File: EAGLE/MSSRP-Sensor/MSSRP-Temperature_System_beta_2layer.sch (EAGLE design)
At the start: 175 parts, among them J1 POWER_JACKPTH, J10 BNCPTH, J11 BNCPTH, J2 USBSMD, J4 TE-2-TERMBLOCK, J5 TE-2-TERMBLOCK, J6 TE-2-TERMBLOCK, J7 TE-2-TERMBLOCK, J8 BNCPTH, J9 BNCPTH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

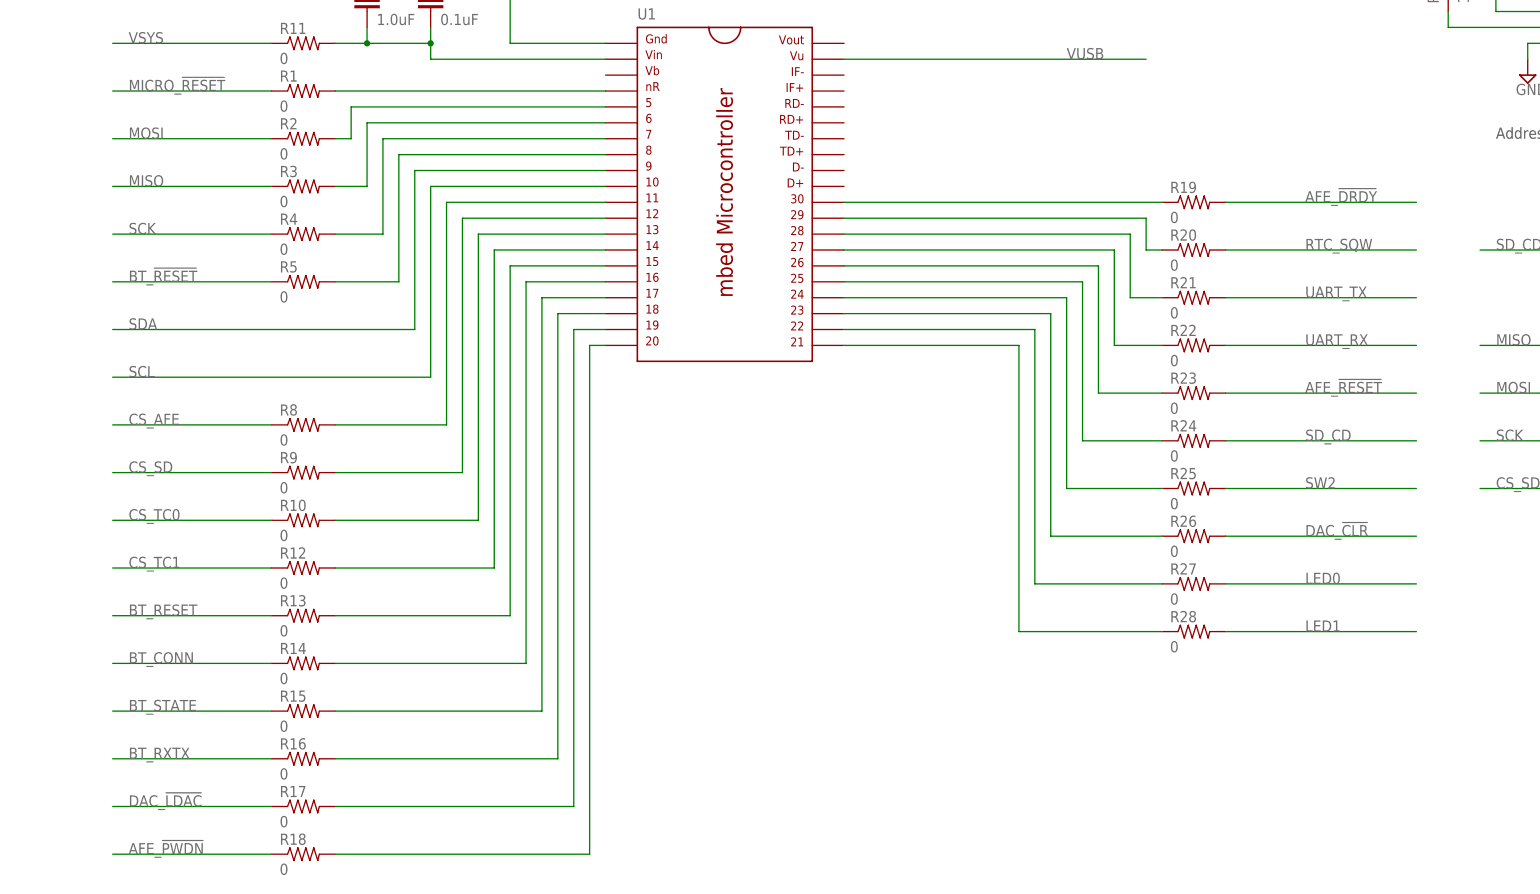
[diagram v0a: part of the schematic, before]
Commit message: 2-layer routing
Finished 2-layer routing tasks
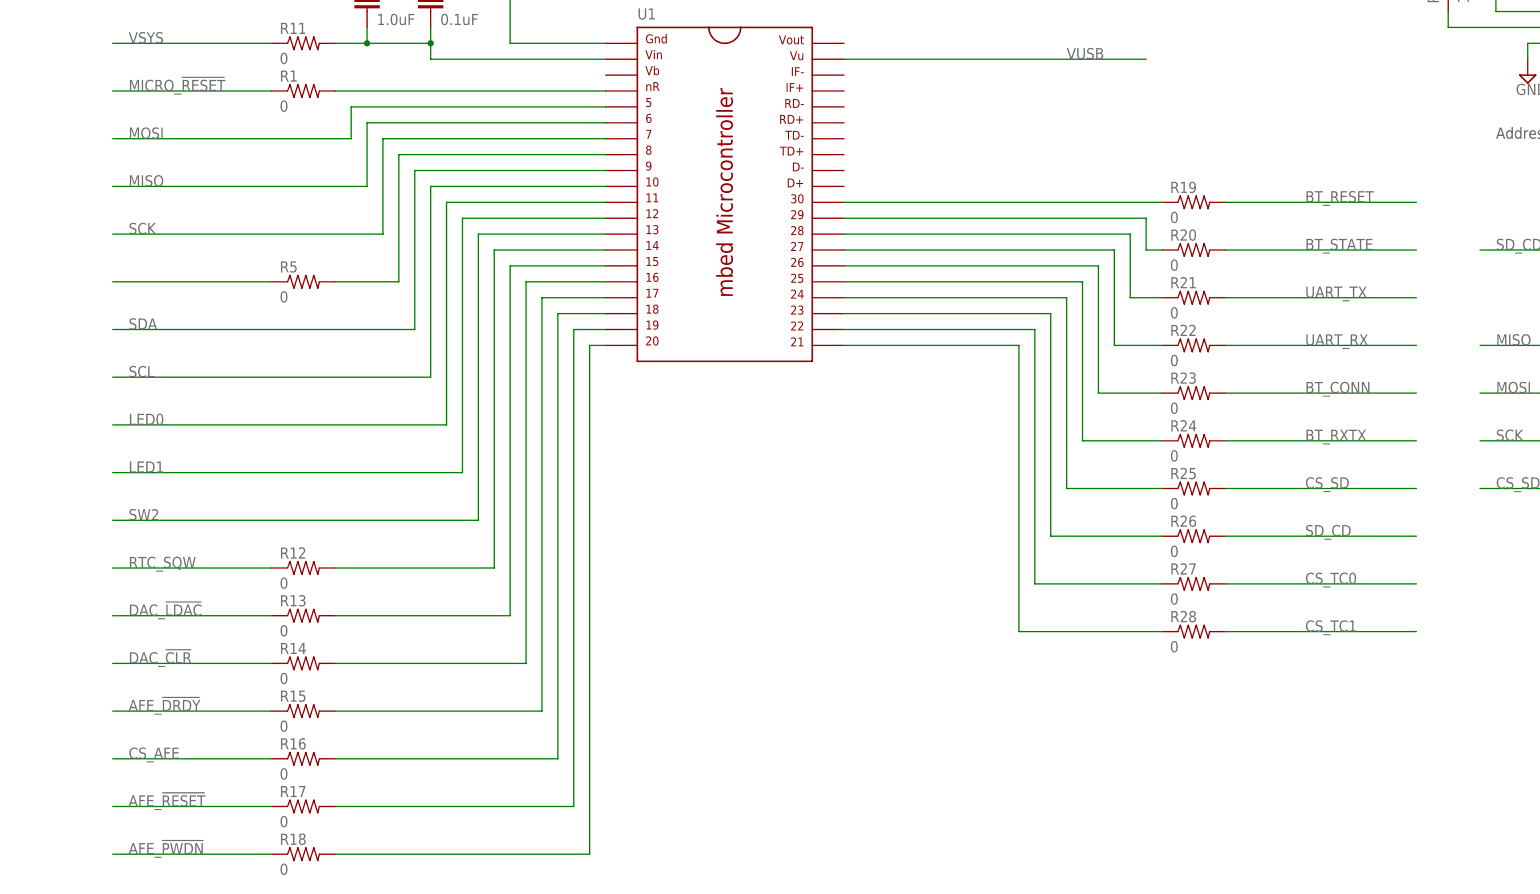
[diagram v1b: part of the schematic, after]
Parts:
- removed R10, R2, R3, R4, R8, R9: 0, SparkFun-Resistors:0OHM1/10W5%(0603)
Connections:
- removed net N$10: R9.2, U1.P$12
- removed net N$11: R10.2, U1.P$13
- removed net N$3: R3.2, U1.P$6
- removed net N$4: R4.2, U1.P$7
- removed net N$9: R8.2, U1.P$11
- net AFE_!DRDY: now also R15.1; no longer R19.2
- net AFE_!RESET: now also R17.1; no longer R23.2
- net BT_!RESET: no longer R5.1
- net BT_CONN: now also R23.2; no longer R14.1
- net BT_RESET: now also R19.2; no longer R13.1
- net BT_RXTX: now also R24.2; no longer R16.1
- net BT_STATE: now also R20.2; no longer R15.1
- net CS_AFE: now also R16.1; no longer R8.1
- net CS_SD: now also R25.2; no longer R9.1
- net CS_TC0: now also R27.2; no longer R10.1
- net CS_TC1: now also R28.2; no longer R12.1
- net DAC_!CLR: now also R14.1; no longer R26.2
- net DAC_!LDAC: now also R13.1; no longer R17.1
- net LED0: now also U1.P$11; no longer R27.2
- net LED1: now also U1.P$12; no longer R28.2
- net MISO: now also U1.P$6; no longer R3.1
- net MOSI: now also U1.P$5; no longer R2.1
- net N$2: now also R5.1; no longer R2.2, U1.P$5
- net RTC_SQW: now also R12.1; no longer R20.2
- net SCK: now also U1.P$7; no longer R4.1
- net SD_CD: now also R26.2; no longer R24.2
- net SW2: now also U1.P$13; no longer R25.2

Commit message: Final Beta
Finished schematic checks and routing adjustments. Boards ready for
initial CAM.
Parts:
- removed R35, R36, R37, R38: 10K, SparkFun-Resistors:10KOHM1/10W1%(0603)0603
- added C36, C52, C54: 10nF, SparkFun-Capacitors:10NF/10000PF-50V-10%(0603)
- added C53, C55: 47uF, SparkFun-Capacitors:47UF-10V-10%(TANT)
- added C56: 22uF, SparkFun-Capacitors:22UF-6.3V-20%(0805)
- added C57: 22uF, SparkFun-Capacitors:22UF-16V-20%-(1210)
- added C58: 1.0uF, SparkFun-Capacitors:1.0UF-16V-10%(0603)
- added R2, R3, R4: 0, SparkFun-Resistors:0OHM1/10W5%(0603)
- added R6, R7, R8, R9: 33OHM, SparkFun-Resistors:33OHM1/10W1%(0603)
- C3: value 0.1uF -> 10nF; device SparkFun-Capacitors:0.1UF-25V-5%(0603) -> SparkFun-Capacitors:10NF/10000PF-50V-10%(0603)
- C33, C8: value 4.7uF -> 10uF; device SparkFun-Capacitors:4.7UF-6.3V-10%(0603)0603 -> SparkFun-Capacitors:10UF-6.3V-20%(0603)
- R16, R55, R56: value 0 -> 100; device SparkFun-Resistors:0OHM1/10W5%(0603) -> SparkFun-Resistors:100OHM1/10W1%(0603)
- R45, R46, R47: value 390 -> 68
- R98, R99: value 470 -> 68
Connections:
- removed net BT_!RESET: C3.1, R38.2, U2.PIO4
- removed net N$35: R35.2, U2.PIO9
- removed net N$36: R36.2, U2.PIO10
- removed net N$37: R37.2, U2.PIO11
- removed net UART_CTS: U2.UARTCTS
- removed net UART_RTS: U2.UARTRTS
- new net N$10: C36.2, C54.1, R8.2, U4.AIN2
- new net N$11: C36.1, R9.2, U4.AIN3
- new net N$3: J2.D+, R2.2
- new net N$4: J2.VBUS, R4.2
- new net N$7: C3.1, R7.2, U4.AIN1
- new net N$9: C3.2, C52.1, R6.2, U4.AIN0
- new net USB_N: R3.1, U1.P$32
- new net USB_P: R2.1, U1.P$31
- net 3.3V: now also C53.+
- net 5V: now also C55.+
- net AFE_AIN0: now also R6.1; no longer U4.AIN0
- net AFE_AIN1: now also R7.1; no longer U4.AIN1
- net AFE_AIN2: now also R8.1; no longer U4.AIN2
- net AFE_AIN3: now also R9.1; no longer U4.AIN3
- net CS_DAC: now also R5.1
- net GND: now also C52.2, C53.-, C54.2, C55.-, C56.2, C57.2, C58.2; no longer C3.2, R35.1, R36.1, R37.1, R38.1
- net N$2: now also J2.D-, R3.2; no longer R5.1
- net VIN: now also C57.1, C58.1
- net VSYS: now also C56.1
- net VUSB: now also R4.1
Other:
- note added: "32.768 kHz"
- note added: "7.68 MHz"
- note added: "DAC7562"
- note added: "DIL SOCKET Row: 26.67 mm Pitch: 2.54 mm"
- note added: "LP2989AIM-3.3"
- note added: "LP2989AIM-5.0"
- note added: "MAX31855T"
- note added: "MAX8934A"
- note added: "MICRO-SD Socket"
- note added: "U10"
- moved on the sheet: C3, J1, R39, R73

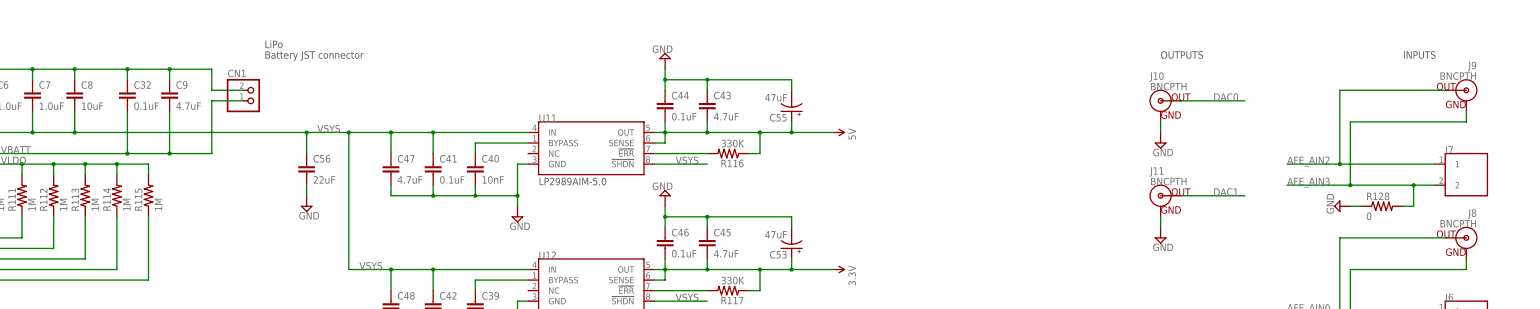
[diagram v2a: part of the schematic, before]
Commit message: DRC and Power pin
Adjustments to pass DRC: miscellaneous clearance issues and
double-drill issue with dual connector footprint.

Also added pin header connection (JP1) to VSYS as a battery system
bypass option for testing.
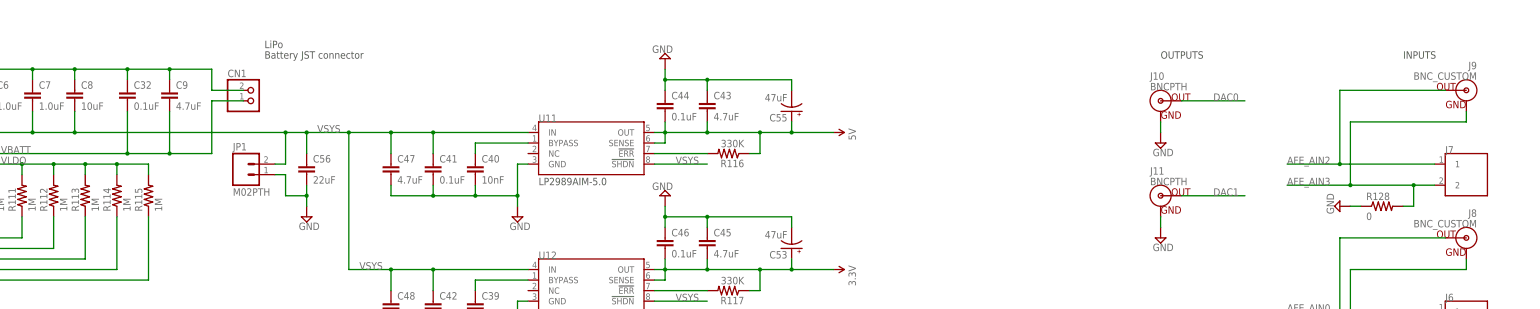
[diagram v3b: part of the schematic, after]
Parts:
- added JP1: M02PTH, SparkFun-Connectors:M02PTH
- J8, J9: value BNCPTH -> BNC_CUSTOM; device SparkFun-Connectors:BNCPTH -> MSSRP-Lib:BNC_CUSTOM
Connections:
- net GND: now also JP1.1
- net VSYS: now also JP1.2
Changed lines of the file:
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@@
 <part name="J11" library="SparkFun-Connectors" deviceset="BNC" device="PTH"/>
 <part name="J10" library="SparkFun-Connectors" deviceset="BNC" device="PTH"/>
-<part name="J9" library="SparkFun-Connectors" deviceset="BNC" device="PTH"/>
-<part name="J8" library="SparkFun-Connectors" deviceset="BNC" device="PTH"/>
+<part name="J9" library="MSSRP-Lib" deviceset="BNC_CUSTOM" device=""/>
+<part name="J8" library="MSSRP-Lib" deviceset="BNC_CUSTOM" device=""/>
 <part name="U$1" library="adafruit" deviceset="MICROSD" device=""/>
 <part name="C15" library="SparkFun-Capacitors" deviceset="4.7UF-6.3V-10%(0603)" device="0603" value="4.7uF"/>
@@
 <part name="C57" library="SparkFun-Capacitors" deviceset="22UF-16V-20%-(1210)" device="" value="22uF"/>
 <part name="C58" library="SparkFun-Capacitors" deviceset="1.0UF-16V-10%(0603)" device="" value="1.0uF"/>
+<part name="JP1" library="SparkFun-Connectors" deviceset="M02" device="PTH"/>
 </parts>
 <sheets>
@@
 <instance part="C53" gate="G$1" x="375.92" y="368.3" rot="R180"/>
 <instance part="C55" gate="G$1" x="375.92" y="401.32" rot="R180"/>
-<instance part="SUPPLY21" gate="GND" x="259.08" y="378.46"/>
+<instance part="SUPPLY21" gate="GND" x="259.08" y="375.92"/>
 <instance part="C56" gate="G$1" x="259.08" y="386.08"/>
 <instance part="C57" gate="G$1" x="520.7" y="289.56"/>
 <instance part="C58" gate="G$1" x="530.86" y="289.56"/>
+<instance part="JP1" gate="G$1" x="243.84" y="386.08"/>
 </instances>
 <busses>
@@
 <pinref part="SUPPLY21" gate="GND" pin="GND"/>
 <wire x1="259.08" y1="383.54" x2="259.08" y2="381" width="0.1524" layer="91"/>
+<pinref part="JP1" gate="G$1" pin="1"/>
+<wire x1="259.08" y1="381" x2="259.08" y2="378.46" width="0.1524" layer="91"/>
+<wire x1="251.46" y1="386.08" x2="254" y2="386.08" width="0.1524" layer="91"/>
+<wire x1="254" y1="386.08" x2="254" y2="381" width="0.1524" layer="91"/>
+<wire x1="254" y1="381" x2="259.08" y2="381" width="0.1524" layer="91"/>
+<junction x="259.08" y="381"/>
 </segment>
 </net>
@@
 <junction x="203.2" y="396.24"/>
 <label x="261.62" y="396.24" size="1.778" layer="95"/>
-<wire x1="203.2" y1="396.24" x2="259.08" y2="396.24" width="0.1524" layer="91"/>
+<wire x1="203.2" y1="396.24" x2="254" y2="396.24" width="0.1524" layer="91"/>
 <pinref part="U11" gate="G$1" pin="IN"/>
 <pinref part="C41" gate="G$1" pin="1"/>
+<wire x1="254" y1="396.24" x2="259.08" y2="396.24" width="0.1524" layer="91"/>
 <wire x1="259.08" y1="396.24" x2="269.24" y2="396.24" width="0.1524" layer="91"/>
 <wire x1="269.24" y1="396.24" x2="279.4" y2="396.24" width="0.1524" layer="91"/>
@@
 <wire x1="259.08" y1="396.24" x2="259.08" y2="391.16" width="0.1524" layer="91"/>
 <junction x="259.08" y="396.24"/>
-</segment>
-<segment>
+<pinref part="JP1" gate="G$1" pin="2"/>
+<wire x1="251.46" y1="388.62" x2="254" y2="388.62" width="0.1524" layer="91"/>
+<wire x1="254" y1="388.62" x2="254" y2="396.24" width="0.1524" layer="91"/>
+<junction x="254" y="396.24"/>
+</segment>
+<segment>
